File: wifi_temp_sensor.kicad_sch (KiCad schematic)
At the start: 9 parts, among them J1 USB_B_Mini, J2 Conn_02x04_Odd_Even, J3 Conn_01x04, J4 Conn_01x06, J6 Conn_01x01, J8 Conn_01x01, SW1 SW_DIP_x01

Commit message: semi complete schematic
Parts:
- removed 3_3VOUT1, 5VIN1, J6, J8: Conn_01x01, Connector_PinSocket_2.54mm:PinSocket_1x01_P2.54mm_Vertical, symbol Connector_Generic:Conn_01x01
- removed J1: USB_B_Mini, Connector_USB:USB_Micro-B_Molex-105017-0001, symbol Connector:USB_B_Mini
- removed J2: Conn_02x04_Odd_Even, Connector_PinSocket_2.54mm:PinSocket_2x04_P2.54mm_Vertical, symbol Connector_Generic:Conn_02x04_Odd_Even
- removed J3: Conn_01x04, Connector_PinSocket_2.54mm:PinSocket_1x04_P2.54mm_Horizontal, symbol Connector_Generic:Conn_01x04
- removed J4: Conn_01x06, Connector_PinHeader_2.54mm:PinHeader_1x06_P2.54mm_Vertical, symbol Connector_Generic:Conn_01x06
- removed SW1: SW_DIP_x01, Button_Switch_THT:SW_PUSH_6mm, symbol Switch:SW_DIP_x01
- added C1, C2, C3: C_Small, symbol Device:C_Small
- added D1: D_Schottky, symbol Device:D_Schottky
- added D2: LED_Small, symbol Device:LED_Small
- added IC1: ESP32-C3-WROOM-02-N4, ESP32C3WROOM02N4, symbol ESP32-C3-WROOM-02-N4:ESP32-C3-WROOM-02-N4
- added IC2: BQ21040DBVR, SOT95P280X145-6N, symbol BQ21040DBVR:BQ21040DBVR
- added J1: USB_C_Receptacle_USB2.0, Connector_USB:USB_C_Receptacle_Molex_105450-0101, symbol Connector:USB_C_Receptacle_USB2.0
- added J2: Batt_Conn, Connector_JST:JST_ACH_BM02B-ACHSS-GAN-ETF_1x02-1MP_P1.20mm_Vertical, symbol Connector:Conn_01x02_Socket
- added L1: L_Small, symbol Device:L_Small
- added Q1, Q2: BF545A, Package_TO_SOT_SMD:SOT-23, symbol Transistor_FET:BF545A
- added R1, R10, R2, R5, R6, R7, R8, R9: R_Small, symbol Device:R_Small
- added R3, R4: 10k, symbol Device:R_Small
- added SW1: SW_SPST, symbol Switch:SW_SPST
- added U1: SHT4x, Sensor_Humidity:Sensirion_DFN-4_1.5x1.5mm_P0.8mm_SHT4x_NoCentralPad, symbol Sensor_Humidity:SHT4x
- added U2: TLV62569DBV, Package_TO_SOT_SMD:SOT-23-5, symbol Regulator_Switching:TLV62569DBV
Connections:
- net +3.3V: now also C2.1, IC1.1 (3V3), L1.2, R3.1, R4.1, R7.1, U1.3 (VDD)
- net GND: now also C1.2, C2.2, C3.2, IC1.19 (GND_2), IC1.20 (GND_3), IC1.21 (GND_4), IC1.22 (GND_5), IC1.23 (GND_6), IC1.24 (GND_7), IC1.25 (GND_8), IC1.26 (GND_9), IC1.27 (GND_10), IC1.9 (GND_1), IC2.5 (GND), J1.A1 (GND), J1.A12 (GND), J1.B1 (GND), J1.B12 (GND), J2.1 (Pin_1), Q1.1 (S), R5.2, R8.2, R9.2, U1.4 (VSS), U2.2 (GND)
- net SDA: now also IC1.17 (IO1), R4.2, U1.1 (SDA)
- new net: C1.1, D1.1 (K), Q2.1 (S), U2.1 (EN), U2.4 (VIN)
- new net: D2.1 (K), IC2.3 (~{CHG})
- new net: D2.2 (A), R10.2
- new net: Q2.3 (G), R5.1, R6.2
- new net: L1.1, U2.3 (SW)
- new net: R7.2, R8.1, U2.5 (FB)
- new net: IC2.4 (ISET), R9.1
- new net: J2.2 (Pin_2), SW1.1 (A)
- new net: Q1.2 (D), R1.2
- new net CHG_ENABLE: IC1.7 (IO8)
- new net D+: IC1.14 (IO19), J1.A6 (D+), J1.B6 (D+)
- new net D-: IC1.13 (IO18), J1.A7 (D-), J1.B7 (D-)
- new net SDC: IC1.18 (IO0), R3.2, U1.2 (SCL)
- new net VBAT_MEAS_EN: IC1.4 (IO5), Q1.3 (G)
- new net V_BAT: IC2.2 (OUT), Q2.2 (D), R10.1, R2.1, SW1.2 (B)
- new net V_BAT_MEAS: IC1.15 (IO3), R1.1, R2.2
- new net V_USB: C3.1, D1.2 (A), IC2.6 (VIN), J1.A4 (VBUS), J1.A9 (VBUS), J1.B4 (VBUS), J1.B9 (VBUS), R6.1
- no-connect marks 7 -> 15

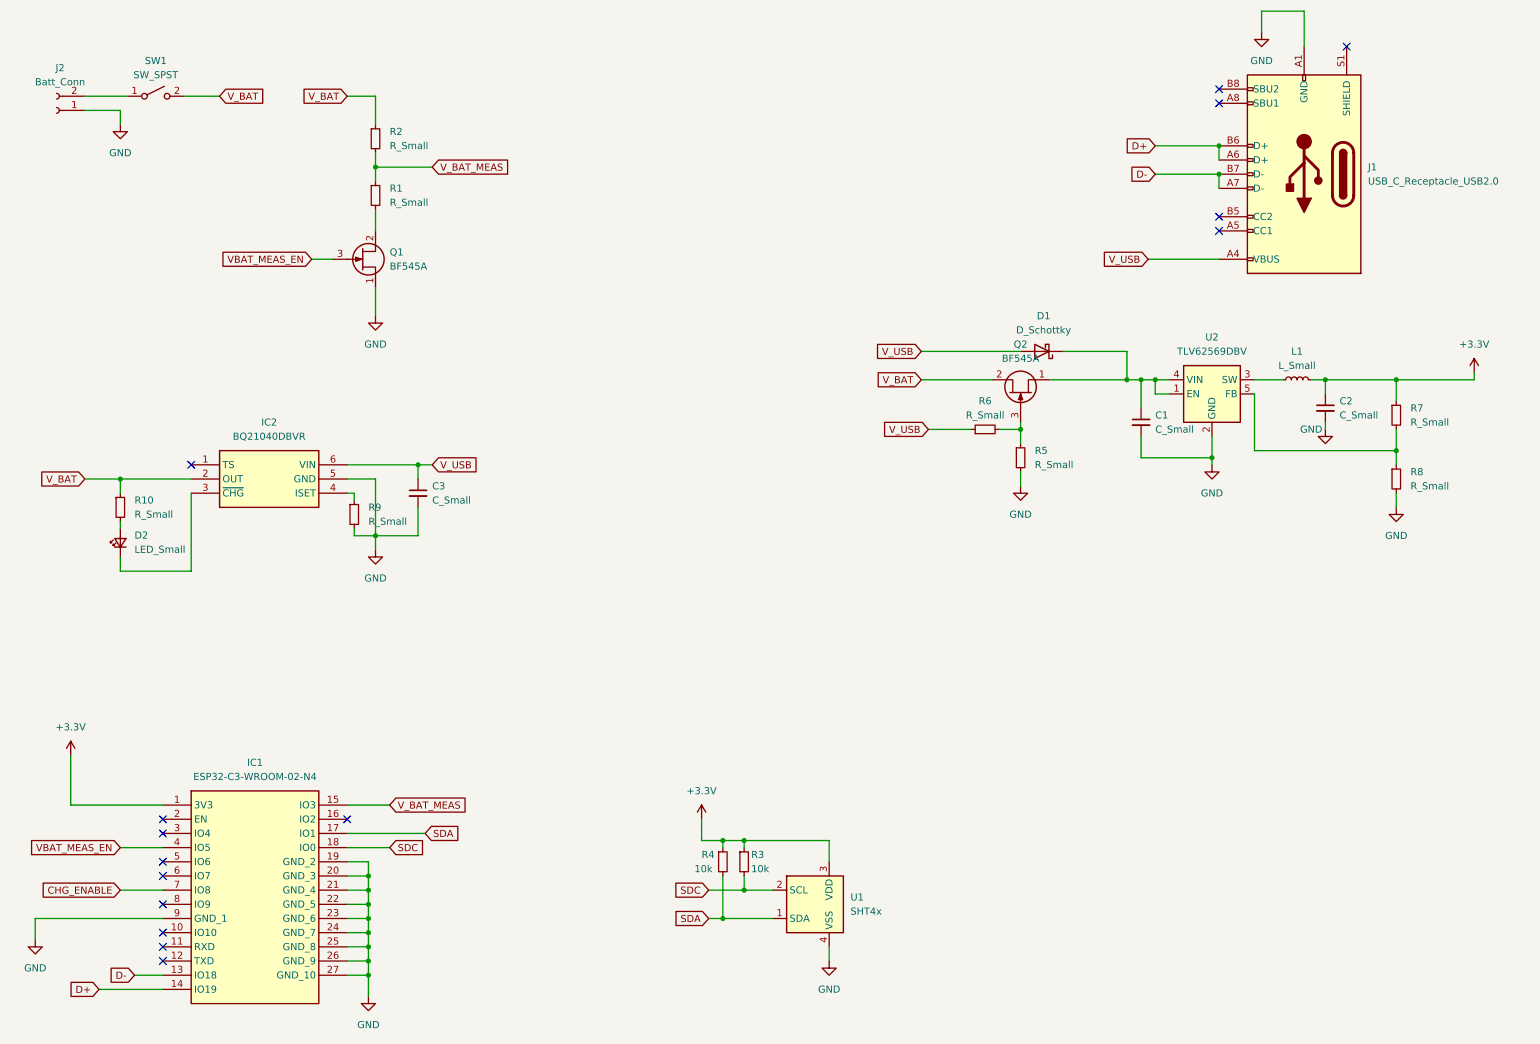
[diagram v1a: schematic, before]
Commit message: Schematic changes to fix issues spotted with some suggestions and improvements
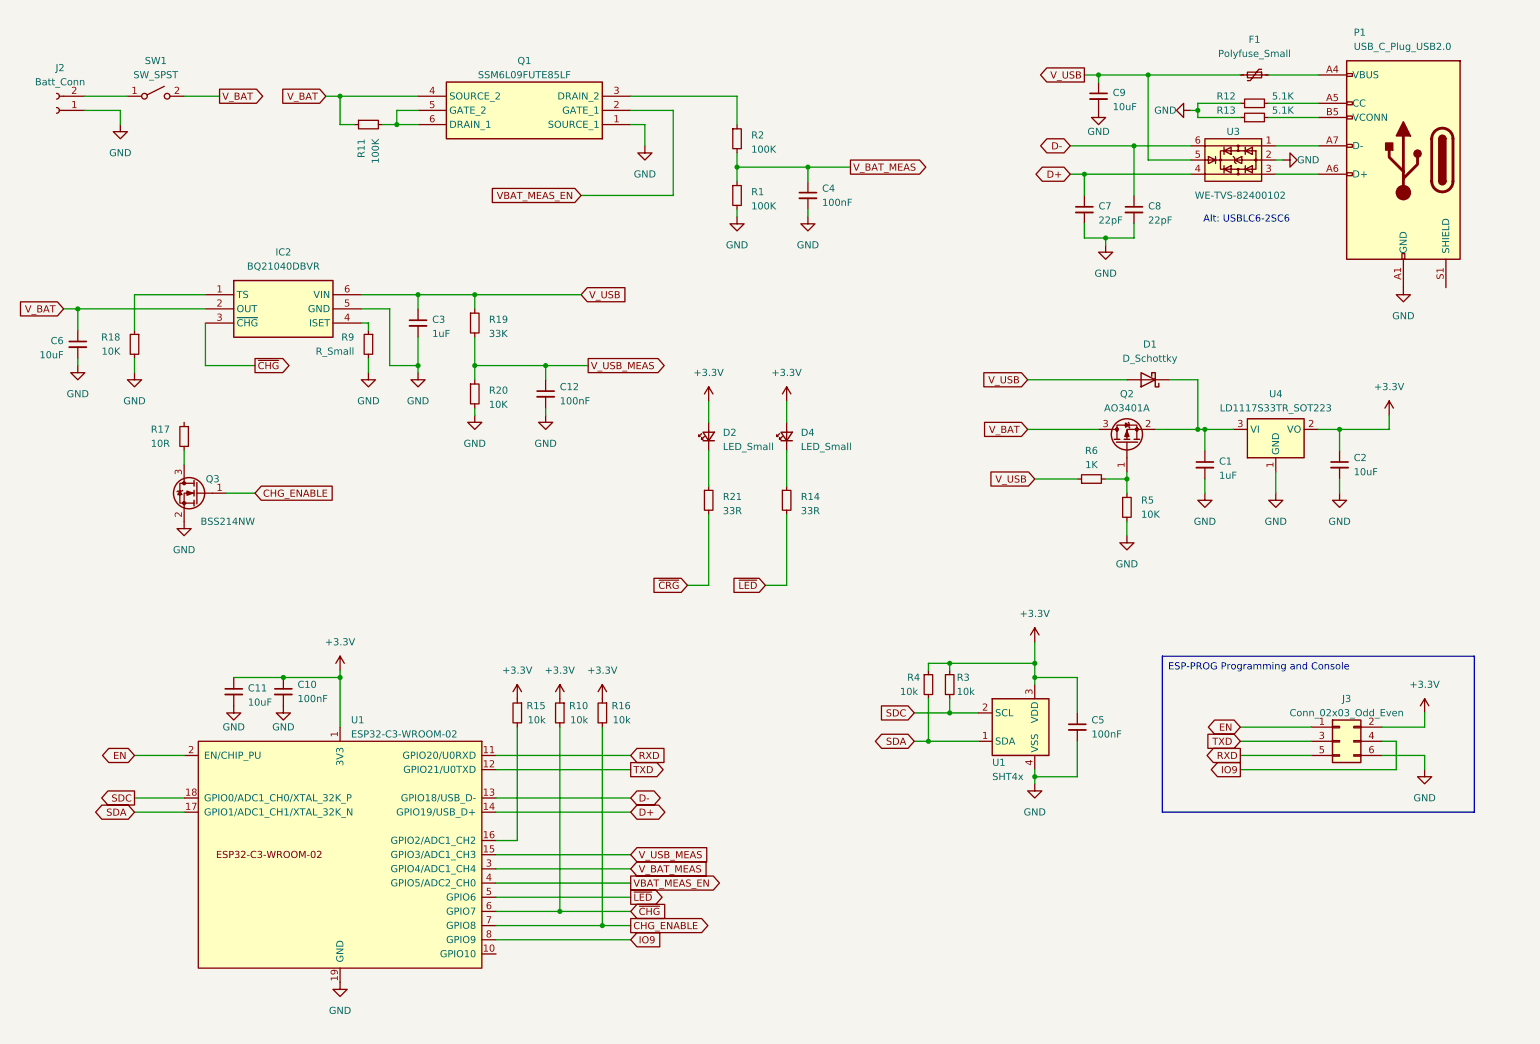
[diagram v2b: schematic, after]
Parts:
- removed IC1: ESP32-C3-WROOM-02-N4, ESP32C3WROOM02N4, symbol ESP32-C3-WROOM-02-N4:ESP32-C3-WROOM-02-N4
- removed J1: USB_C_Receptacle_USB2.0, Connector_USB:USB_C_Receptacle_Molex_105450-0101, symbol Connector:USB_C_Receptacle_USB2.0
- removed L1: L_Small, symbol Device:L_Small
- removed Q1, Q2: BF545A, Package_TO_SOT_SMD:SOT-23, symbol Transistor_FET:BF545A
- removed R7, R8: R_Small, symbol Device:R_Small
- removed U2: TLV62569DBV, Package_TO_SOT_SMD:SOT-23-5, symbol Regulator_Switching:TLV62569DBV
- added C10: 100nF, Capacitor_SMD:C_0603_1608Metric, symbol Device:C_Small
- added C11, C6, C9: 10uF, Capacitor_SMD:C_0805_2012Metric, symbol Device:C_Small
- added C12, C4, C5: 100nF, symbol Device:C_Small
- added C7, C8: 22pF, symbol Device:C_Small
- added D4: LED_Small, LED_SMD:LED_0603_1608Metric, symbol Device:LED_Small
- added F1: Polyfuse_Small, symbol Device:Polyfuse_Small
- added J3: Conn_02x03_Odd_Even, Connector_PinHeader_1.27mm:PinHeader_2x03_P1.27mm_Vertical, symbol Connector_Generic:Conn_02x03_Odd_Even
- added P1: USB_C_Plug_USB2.0, Connector_USB:USB_C_Receptacle_Palconn_UTC16-G, symbol Connector:USB_C_Plug_USB2.0
- added Q1: SSM6L09FUTE85LF, SamacSys_parts:SOT65P210X120-6N, symbol SamacSys_parts:SSM6L09FUTE85LF
- added Q2: AO3401A, Package_TO_SOT_SMD:SOT-23, symbol Transistor_FET:AO3401A
- added Q3: BSS214NW, Package_TO_SOT_SMD:SOT-323_SC-70, symbol Transistor_FET:BSS214NW
- added R11: 100K, Resistor_SMD:R_0402_1005Metric, symbol Device:R_Small
- added R12, R13: 5.1K, symbol Device:R_Small
- added R14, R21: 33R, Resistor_SMD:R_0603_1608Metric, symbol Device:R_Small
- added R15, R16: 10k, symbol Device:R_Small
- added R17: 10R, symbol Device:R_Small
- added R18: 10K, Resistor_SMD:R_0603_1608Metric, symbol Device:R_Small
- added R19: 33K, symbol Device:R_Small
- added R20: 10K, symbol Device:R_Small
- added U1: ESP32-C3-WROOM-02, PCM_Espressif:ESP32-C3-WROOM-02, symbol PCM_Espressif:ESP32-C3-WROOM-02
- added U3: WE-TVS-82400102, Package_TO_SOT_SMD:SOT-23-6, symbol Power_Protection:WE-TVS-82400102
- added U4: LD1117S33TR_SOT223, Package_TO_SOT_SMD:SOT-223-3_TabPin2, symbol Regulator_Linear:LD1117S33TR_SOT223
- C1: value C_Small -> 1uF
- C2: value C_Small -> 10uF; footprint (none) -> Capacitor_SMD:C_0805_2012Metric
- C3: value C_Small -> 1uF; footprint (none) -> Capacitor_SMD:C_0603_1608Metric
- D2: footprint (none) -> LED_SMD:LED_0603_1608Metric
- R1, R2: value R_Small -> 100K
- R10: value R_Small -> 10k
- R5: value R_Small -> 10K; footprint (none) -> Resistor_SMD:R_0603_1608Metric
- R6: value R_Small -> 1K; footprint (none) -> Resistor_SMD:R_0603_1608Metric
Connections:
- net +3.3V: now also D2.2 (A), R10.1, C10.1, C11.1, C5.1, D4.2 (A), J3.2 (Pin_2), R15.1, R16.1, U1.1 (3V3), U4.2 (VO)
- net CHG_ENABLE: now also Q3.1 (G), R16.2, U1.7 (GPIO8)
- net D+: now also C7.1, U1.14 (GPIO19/USB_D+), U3.4
- net D-: now also C8.1, U1.13 (GPIO18/USB_D-), U3.6
- net GND: now also R1.2, C10.2, C11.2, C12.2, C4.2, C5.2, C6.2, C7.2, C8.2, C9.2, J3.6 (Pin_6), P1.A1 (GND), P1.A12 (GND), P1.B1 (GND), P1.B12 (GND), Q1.1 (SOURCE_1), Q3.2 (S), R12.1, R13.1, R18.2, R20.2, U1.19 (GND), U1.9 (GND), U3.2, U4.1 (GND)
- net SDA: now also U1.17 (GPIO1/ADC1_CH1/XTAL_32K_N)
- net SDC: now also U1.18 (GPIO0/ADC1_CH0/XTAL_32K_P)
- net VBAT_MEAS_EN: now also Q1.2 (GATE_1), U1.4 (GPIO5/ADC2_CH0)
- net V_BAT: now also C6.1, Q1.4 (SOURCE_2), Q2.3 (D), R11.1; no longer R10.1, R2.1
- net V_BAT_MEAS: now also C4.1, U1.3 (GPIO4/ADC1_CH4)
- net V_USB: now also C9.1, F1.2, R19.1, U3.5
- net at C1.1, D1.1 (K): now also Q2.2 (S), U4.3 (VI)
- net at D2.1 (K): now also R21.1; no longer IC2.3 (~{CHG})
- net ~{CHG}: now reaches R10.2
- net ~{CHG}: now also IC2.3 (~{CHG}), U1.6 (GPIO7); no longer D2.2 (A)
- net at R5.1, R6.2: now also Q2.1 (G)
- net at IC2.1 (TS): now also R18.1
- new net: P1.A7 (D-), U3.1
- new net: P1.A6 (D+), U3.3
- new net: F1.1, P1.A4 (VBUS), P1.A9 (VBUS), P1.B4 (VBUS), P1.B9 (VBUS)
- new net: R15.2, U1.16 (GPIO2/ADC1_CH2)
- new net: P1.B5 (VCONN), R13.2
- new net: Q1.3 (DRAIN_2), R2.1
- new net: Q1.5 (GATE_2), Q1.6 (DRAIN_1), R11.2
- new net: P1.A5 (CC), R12.2
- new net: Q3.3 (D), R17.2
- new net: D4.1 (K), R14.1
- new net EN: J3.1 (Pin_1), U1.2 (EN/CHIP_PU)
- new net IO9: J3.4 (Pin_4), U1.8 (GPIO9)
- new net RXD: J3.5 (Pin_5), U1.11 (GPIO20/U0RXD)
- new net TXD: J3.3 (Pin_3), U1.12 (GPIO21/U0TXD)
- new net V_USB_MEAS: C12.1, R19.2, R20.1, U1.15 (GPIO3/ADC1_CH3)
- new net ~{CRG}: R21.2
- new net ~{LED}: R14.2, U1.5 (GPIO6)
- no-connect marks 15 -> 0
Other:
- note added: "Alt: USBLC6-2SC6"
- moved on the sheet: C1, C2, C3, D1, IC2, R1, R2, R3, R4, R5, R6, R9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

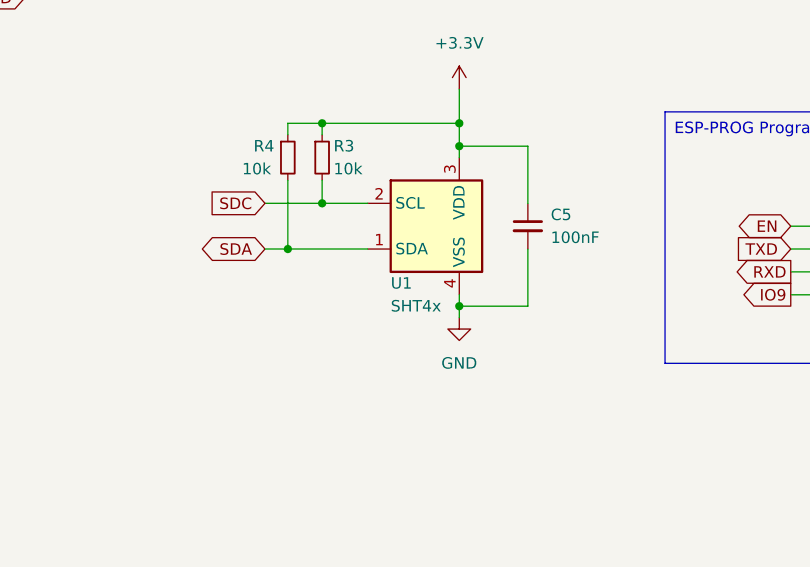
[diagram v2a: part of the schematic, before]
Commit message: Annotated and updated some of the PCB footprints
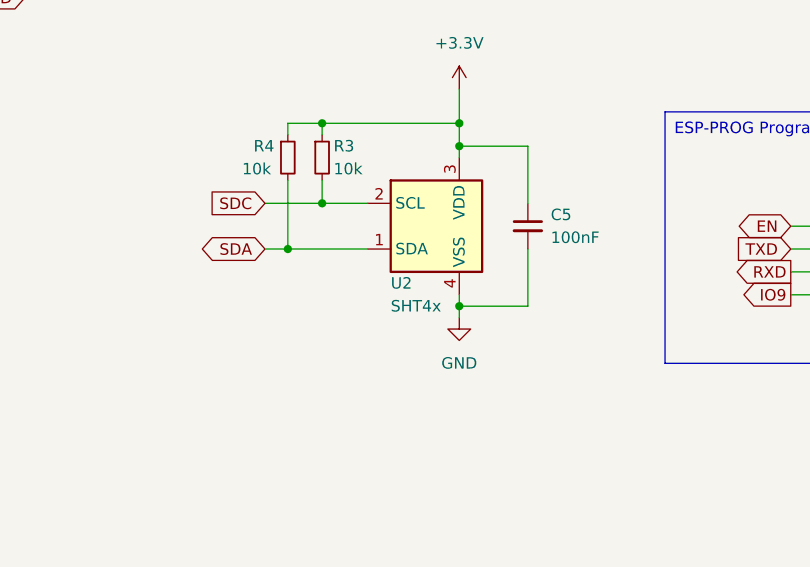
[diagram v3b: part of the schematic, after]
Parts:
- renumbered U1 to U2
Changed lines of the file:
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@@
   (symbol (lib_id "Sensor_Humidity:SHT4x") (at 195.58 140.97 0) (unit 1)
     (in_bom yes) (on_board yes) (dnp no)
-    (property "Reference" "U1" (at 190.5 147.32 0)
+    (property "Reference" "U2" (at 190.5 147.32 0)
       (effects (font (size 1.27 1.27)) (justify left))
     )
@@
       (project "wifi_temp_sensor"
         (path "/f6c77997-b71a-421e-9dbe-7ca9e2d5ccfe"
-          (reference "U1") (unit 1)
+          (reference "U2") (unit 1)
         )
       )
